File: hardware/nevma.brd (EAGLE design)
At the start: 34.6 x 15.9 mm, 9 parts, among them J1 USB_A_PTH_MALE, U1 TINY85-20-DIP

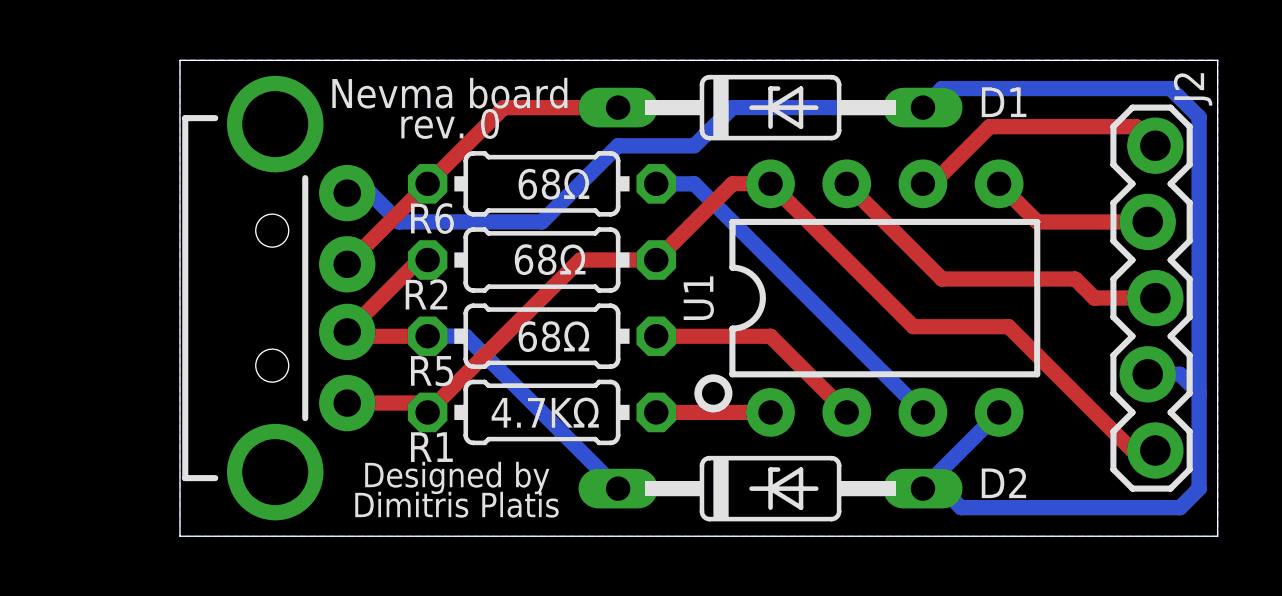
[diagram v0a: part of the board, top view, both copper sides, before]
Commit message: Decrease board size
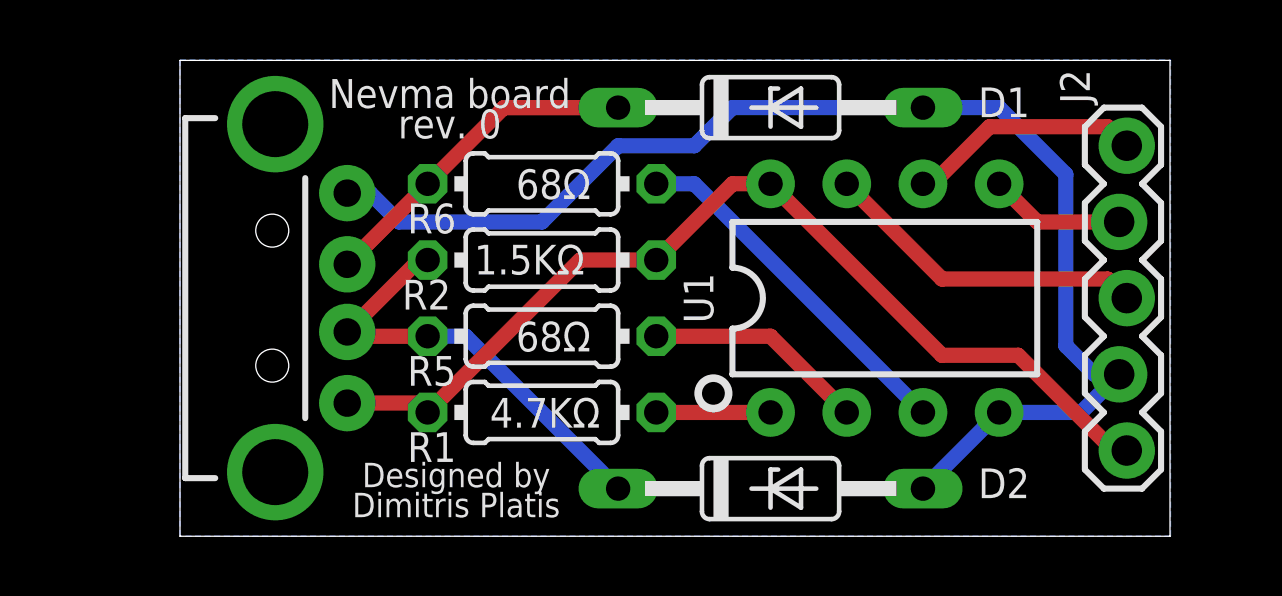
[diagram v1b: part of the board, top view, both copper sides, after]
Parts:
- R2: value 68Ω -> 1.5KΩ
- moved J2 0.95 mm to (70.2, 58.4)
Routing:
- net GND: track 58.7 -> 42.9 mm
- net VCC: track 33.9 -> 33.0 mm
- net SDA: track 5.48 -> 4.53 mm
- net SCL: track 11.9 -> 10.9 mm
- net INT: track 8.80 -> 7.85 mm
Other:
- board size 34.6 x 15.9 mm -> 33 x 15.9 mm
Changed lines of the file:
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@@
 <board>
 <plain>
-<wire x1="38.735" y1="45.4025" x2="73.3225" y2="45.4025" width="0" layer="20"/>
-<wire x1="73.3225" y1="45.4025" x2="73.3225" y2="61.265" width="0" layer="20"/>
-<wire x1="73.3225" y1="61.265" x2="38.735" y2="61.265" width="0" layer="20"/>
+<wire x1="38.735" y1="45.4025" x2="71.735" y2="45.4025" width="0" layer="20"/>
+<wire x1="71.735" y1="45.4025" x2="71.735" y2="61.265" width="0" layer="20"/>
+<wire x1="71.735" y1="61.265" x2="38.735" y2="61.265" width="0" layer="20"/>
 <wire x1="38.735" y1="61.265" x2="38.735" y2="45.4025" width="0" layer="20"/>
-<text x="72.39" y="48.895" size="8.636" layer="22" font="vector" ratio="20" distance="100" rot="MR0">NEVMA</text>
-<text x="47.7266" y="60.6425" size="0.9652" layer="21" font="vector" ratio="20" distance="5" align="top-center">Nevma board
+<text x="71.4375" y="48.895" size="8.636" layer="22" font="vector" ratio="20" distance="100" rot="MR0">NEVMA</text>
+<text x="47.7266" y="60.6425" size="0.9652" layer="21" font="vector" ratio="18" distance="5" align="top-center">Nevma board
 rev. 0</text>
 <text x="47.9425" y="46.0375" size="0.8128" layer="21" font="vector" ratio="10" distance="23" align="bottom-center">Designed by
@@
 <attribute name="VALUE" x="53.9115" y="45.4025" size="0.8128" layer="27" ratio="10"/>
 </element>
-<element name="J2" library="SparkFun-Connectors" library_urn="urn:adsk.eagle:library:513" package="1X05_LOCK" package3d_urn="urn:adsk.eagle:package:38105/1" value="" x="71.12" y="58.42" smashed="yes" rot="R270">
-<attribute name="NAME" x="71.882" y="60.96" size="0.9906" layer="25" font="vector" ratio="20" rot="R270"/>
-<attribute name="VALUE" x="69.088" y="59.69" size="0.6096" layer="27" font="vector" ratio="20" rot="R270"/>
+<element name="J2" library="SparkFun-Connectors" library_urn="urn:adsk.eagle:library:513" package="1X05_LOCK" package3d_urn="urn:adsk.eagle:package:38105/1" value="" x="70.1675" y="58.42" smashed="yes" rot="R270">
+<attribute name="NAME" x="68.072" y="60.96" size="0.9906" layer="25" font="vector" ratio="20" rot="R270"/>
+<attribute name="VALUE" x="68.1355" y="59.69" size="0.6096" layer="27" font="vector" ratio="20" rot="R270"/>
 </element>
 <element name="R1" library="rcl" library_urn="urn:adsk.eagle:library:334" package="0204/7" package3d_urn="urn:adsk.eagle:package:23498/1" value="4.7KΩ" x="50.8" y="49.53" smashed="yes" rot="R180">
@@
 <attribute name="VALUE" x="52.7431" y="50.0126" size="0.9906" layer="25" ratio="10" rot="R180"/>
 </element>
-<element name="R2" library="rcl" library_urn="urn:adsk.eagle:library:334" package="0204/7" package3d_urn="urn:adsk.eagle:package:23498/1" value="68Ω" x="50.8" y="54.61" smashed="yes">
+<element name="R2" library="rcl" library_urn="urn:adsk.eagle:library:334" package="0204/7" package3d_urn="urn:adsk.eagle:package:23498/1" value="1.5KΩ" x="50.8" y="54.61" smashed="yes">
 <attribute name="NAME" x="46.1391" y="52.959" size="0.9906" layer="25" ratio="10"/>
-<attribute name="VALUE" x="49.8094" y="54.1274" size="0.9906" layer="25" ratio="10"/>
+<attribute name="VALUE" x="48.5394" y="54.1274" size="0.9906" layer="25" ratio="10"/>
 </element>
 </elements>
@@
 <contactref element="J2" pad="4"/>
 <contactref element="U1" pad="4"/>
-<wire x1="66.04" y1="49.53" x2="63.5" y2="46.99" width="0.508" layer="16"/>
-<wire x1="72.0725" y1="46.355" x2="72.7075" y2="46.99" width="0.508" layer="16"/>
-<wire x1="72.7075" y1="46.99" x2="72.7075" y2="50.165" width="0.508" layer="16"/>
-<wire x1="72.7075" y1="50.165" x2="72.0725" y2="50.8" width="0.508" layer="16"/>
-<wire x1="72.0725" y1="50.8" x2="70.993" y2="50.8" width="0.508" layer="16"/>
-<wire x1="72.7075" y1="50.165" x2="72.7075" y2="59.3725" width="0.508" layer="16"/>
-<wire x1="72.7075" y1="59.3725" x2="71.755" y2="60.325" width="0.508" layer="16"/>
-<wire x1="71.755" y1="60.325" x2="64.135" y2="60.325" width="0.508" layer="16"/>
-<wire x1="63.5" y1="59.69" x2="64.135" y2="60.325" width="0.508" layer="16"/>
-<wire x1="63.5" y1="46.99" x2="64.135" y2="46.99" width="0.508" layer="16"/>
-<wire x1="64.135" y1="46.99" x2="64.77" y2="46.355" width="0.508" layer="16"/>
-<wire x1="64.77" y1="46.355" x2="72.0725" y2="46.355" width="0.508" layer="16"/>
+<wire x1="63.5" y1="46.99" x2="66.04" y2="49.53" width="0.508" layer="16"/>
 <wire x1="44.31" y1="56.84" x2="45.0775" y2="56.84" width="0.508" layer="16"/>
 <wire x1="45.0775" y1="56.84" x2="46.0375" y2="55.88" width="0.508" layer="16"/>
@@
 <wire x1="53.34" y1="58.42" x2="55.88" y2="58.42" width="0.508" layer="16"/>
 <wire x1="55.88" y1="58.42" x2="57.15" y2="59.69" width="0.508" layer="16"/>
-<wire x1="57.15" y1="59.69" x2="63.5" y2="59.69" width="0.508" layer="16"/>
+<wire x1="63.5" y1="59.69" x2="57.15" y2="59.69" width="0.508" layer="16"/>
+<wire x1="66.04" y1="49.53" x2="68.7705" y2="49.53" width="0.508" layer="16"/>
+<wire x1="68.7705" y1="49.53" x2="70.0405" y2="50.8" width="0.508" layer="16"/>
+<wire x1="70.0405" y1="50.8" x2="69.215" y2="50.8" width="0.508" layer="16"/>
+<wire x1="69.215" y1="50.8" x2="68.2625" y2="51.7525" width="0.508" layer="16"/>
+<wire x1="68.2625" y1="57.4675" x2="66.04" y2="59.69" width="0.508" layer="16"/>
+<wire x1="66.04" y1="59.69" x2="63.5" y2="59.69" width="0.508" layer="16"/>
+<wire x1="68.2625" y1="51.7525" x2="68.2625" y2="57.4675" width="0.508" layer="16"/>
 <polygon width="0.254" layer="16">
 <vertex x="38.735" y="61.2775"/>
-<vertex x="73.3425" y="61.2775"/>
-<vertex x="73.3425" y="45.4025"/>
+<vertex x="71.755" y="61.2775"/>
+<vertex x="71.755" y="45.4025"/>
 <vertex x="38.735" y="45.4025"/>
 </polygon>
@@
 <contactref element="R1" pad="2"/>
 <contactref element="R2" pad="2"/>
-<wire x1="71.247" y1="48.26" x2="70.485" y2="48.26" width="0.508" layer="1"/>
-<wire x1="70.485" y1="48.26" x2="66.3575" y2="52.3875" width="0.508" layer="1"/>
-<wire x1="66.3575" y1="52.3875" x2="63.1825" y2="52.3875" width="0.508" layer="1"/>
-<wire x1="63.1825" y1="52.3875" x2="58.42" y2="57.15" width="0.508" layer="1"/>
-<wire x1="44.31" y1="49.84" x2="46.68" y2="49.84" width="0.508" layer="1"/>
+<wire x1="46.68" y1="49.84" x2="44.31" y2="49.84" width="0.508" layer="1"/>
 <wire x1="46.99" y1="49.53" x2="46.68" y2="49.84" width="0.508" layer="1"/>
 <wire x1="58.42" y1="57.15" x2="57.15" y2="57.15" width="0.508" layer="1"/>
@@
 <wire x1="54.61" y1="54.61" x2="52.07" y2="54.61" width="0.508" layer="1"/>
 <wire x1="52.07" y1="54.61" x2="46.99" y2="49.53" width="0.508" layer="1"/>
+<wire x1="70.2945" y1="48.26" x2="69.85" y2="48.26" width="0.508" layer="1"/>
+<wire x1="69.85" y1="48.26" x2="66.675" y2="51.435" width="0.508" layer="1"/>
+<wire x1="66.675" y1="51.435" x2="64.135" y2="51.435" width="0.508" layer="1"/>
+<wire x1="64.135" y1="51.435" x2="58.42" y2="57.15" width="0.508" layer="1"/>
 </signal>
 <signal name="SDA">
 <contactref element="U1" pad="5"/>
 <contactref element="J2" pad="2"/>
-<wire x1="70.993" y1="55.88" x2="67.31" y2="55.88" width="0.508" layer="1"/>
-<wire x1="67.31" y1="55.88" x2="66.04" y2="57.15" width="0.508" layer="1"/>
+<wire x1="66.04" y1="57.15" x2="67.31" y2="55.88" width="0.508" layer="1"/>
+<wire x1="67.31" y1="55.88" x2="70.0405" y2="55.88" width="0.508" layer="1"/>
 </signal>
 <signal name="SCL">
 <contactref element="U1" pad="7"/>
 <contactref element="J2" pad="3"/>
-<wire x1="71.247" y1="53.34" x2="69.215" y2="53.34" width="0.508" layer="1"/>
-<wire x1="69.215" y1="53.34" x2="68.58" y2="53.975" width="0.508" layer="1"/>
-<wire x1="68.58" y1="53.975" x2="64.135" y2="53.975" width="0.508" layer="1"/>
-<wire x1="64.135" y1="53.975" x2="60.96" y2="57.15" width="0.508" layer="1"/>
+<wire x1="60.96" y1="57.15" x2="64.135" y2="53.975" width="0.508" layer="1"/>
+<wire x1="69.6595" y1="53.975" x2="70.2945" y2="53.34" width="0.508" layer="1"/>
+<wire x1="64.135" y1="53.975" x2="69.6595" y2="53.975" width="0.508" layer="1"/>
 </signal>
 <signal name="INT">
 <contactref element="J2" pad="1"/>
 <contactref element="U1" pad="6"/>
-<wire x1="71.247" y1="58.42" x2="70.612" y2="59.055" width="0.508" layer="1"/>
-<wire x1="70.612" y1="59.055" x2="65.7225" y2="59.055" width="0.508" layer="1"/>
+<wire x1="70.2945" y1="58.42" x2="69.6595" y2="59.055" width="0.508" layer="1"/>
+<wire x1="69.6595" y1="59.055" x2="65.7225" y2="59.055" width="0.508" layer="1"/>
 <wire x1="65.7225" y1="59.055" x2="63.8175" y2="57.15" width="0.508" layer="1"/>
 <wire x1="63.8175" y1="57.15" x2="63.5" y2="57.15" width="0.508" layer="1"/>

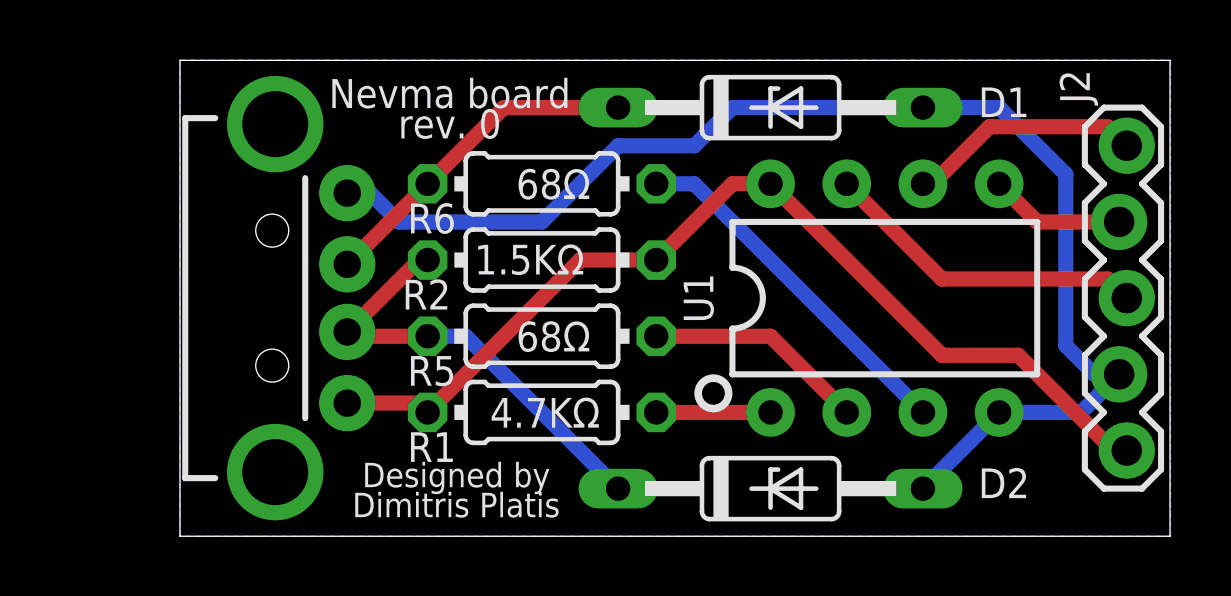
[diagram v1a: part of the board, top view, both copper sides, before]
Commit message: Reduce board size This will allower the better fit of the USB socket
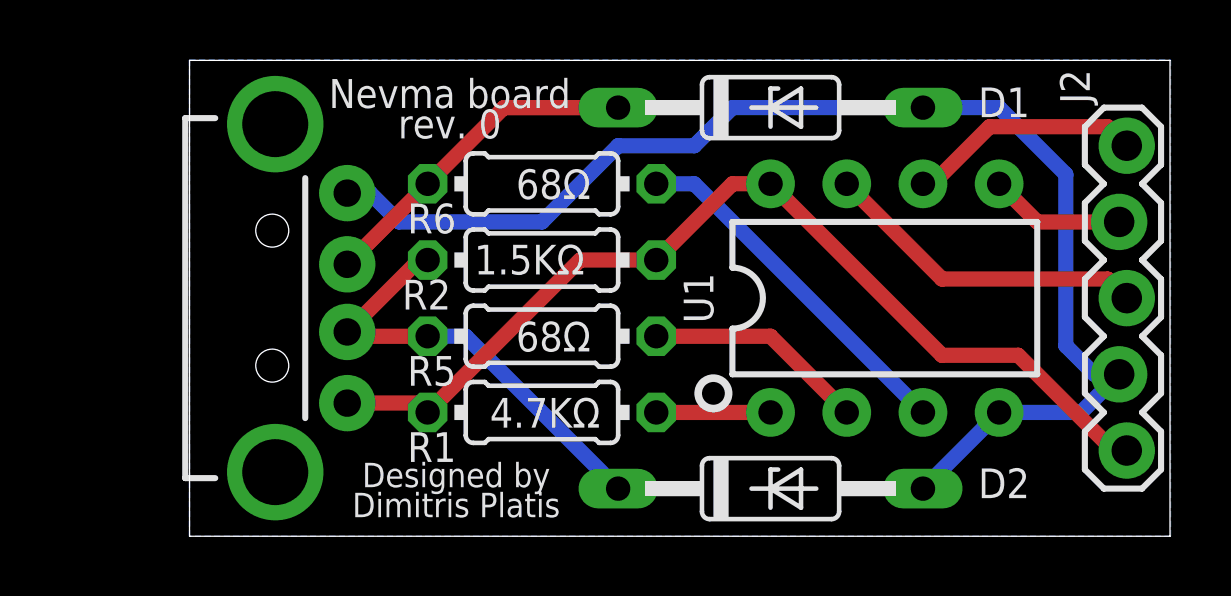
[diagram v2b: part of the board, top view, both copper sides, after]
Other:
- board size 33 x 15.9 mm -> 32.7 x 15.9 mm
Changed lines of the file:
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@@
 <board>
 <plain>
-<wire x1="38.735" y1="45.4025" x2="71.735" y2="45.4025" width="0" layer="20"/>
+<wire x1="39.0525" y1="45.4025" x2="71.735" y2="45.4025" width="0" layer="20"/>
 <wire x1="71.735" y1="45.4025" x2="71.735" y2="61.265" width="0" layer="20"/>
-<wire x1="71.735" y1="61.265" x2="38.735" y2="61.265" width="0" layer="20"/>
-<wire x1="38.735" y1="61.265" x2="38.735" y2="45.4025" width="0" layer="20"/>
+<wire x1="71.735" y1="61.265" x2="39.0525" y2="61.265" width="0" layer="20"/>
+<wire x1="39.0525" y1="61.265" x2="39.0525" y2="45.4025" width="0" layer="20"/>
 <text x="71.4375" y="48.895" size="8.636" layer="22" font="vector" ratio="20" distance="100" rot="MR0">NEVMA</text>
 <text x="47.7266" y="60.6425" size="0.9652" layer="21" font="vector" ratio="18" distance="5" align="top-center">Nevma board
@@
 <wire x1="68.2625" y1="51.7525" x2="68.2625" y2="57.4675" width="0.508" layer="16"/>
 <polygon width="0.254" layer="16">
-<vertex x="38.735" y="61.2775"/>
+<vertex x="39.0525" y="61.2775"/>
 <vertex x="71.755" y="61.2775"/>
 <vertex x="71.755" y="45.4025"/>
-<vertex x="38.735" y="45.4025"/>
+<vertex x="39.0525" y="45.4025"/>
 </polygon>
 </signal>

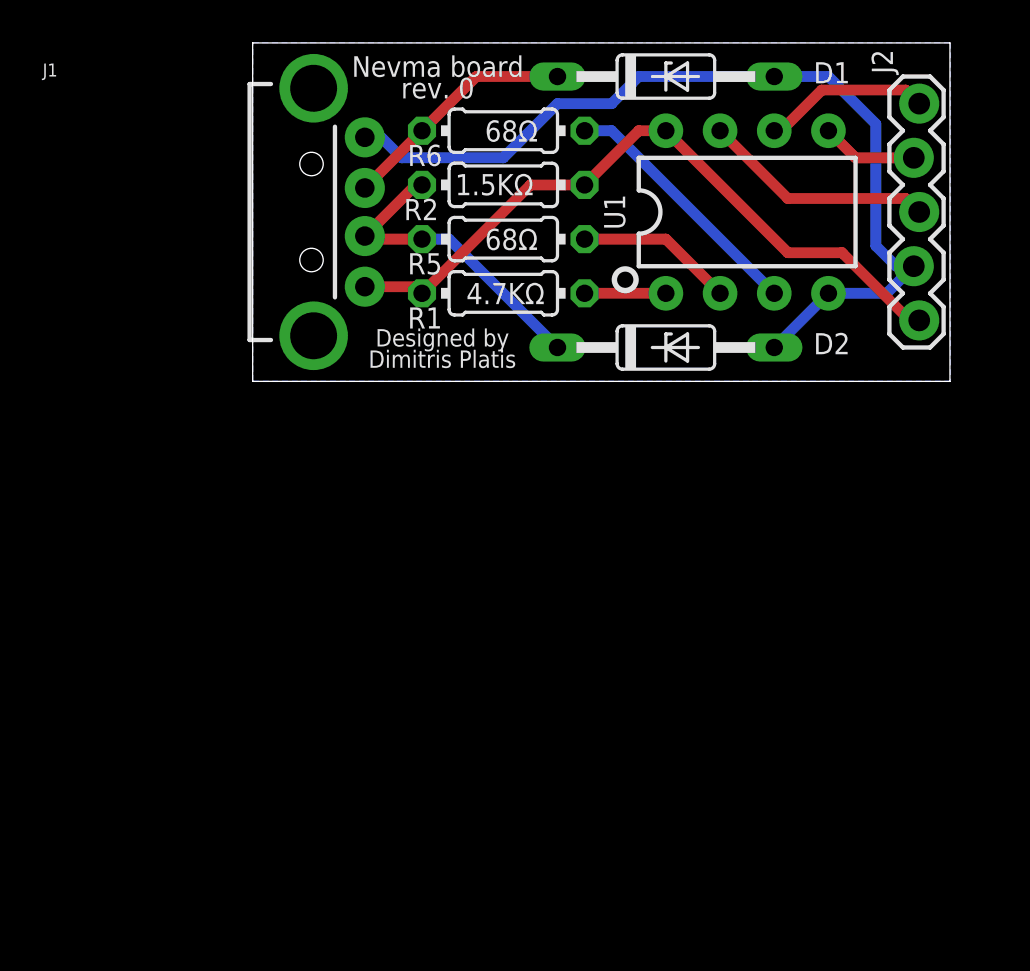
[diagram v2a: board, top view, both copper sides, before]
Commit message: New concept based on atmega32u4 board
HW rev. 2
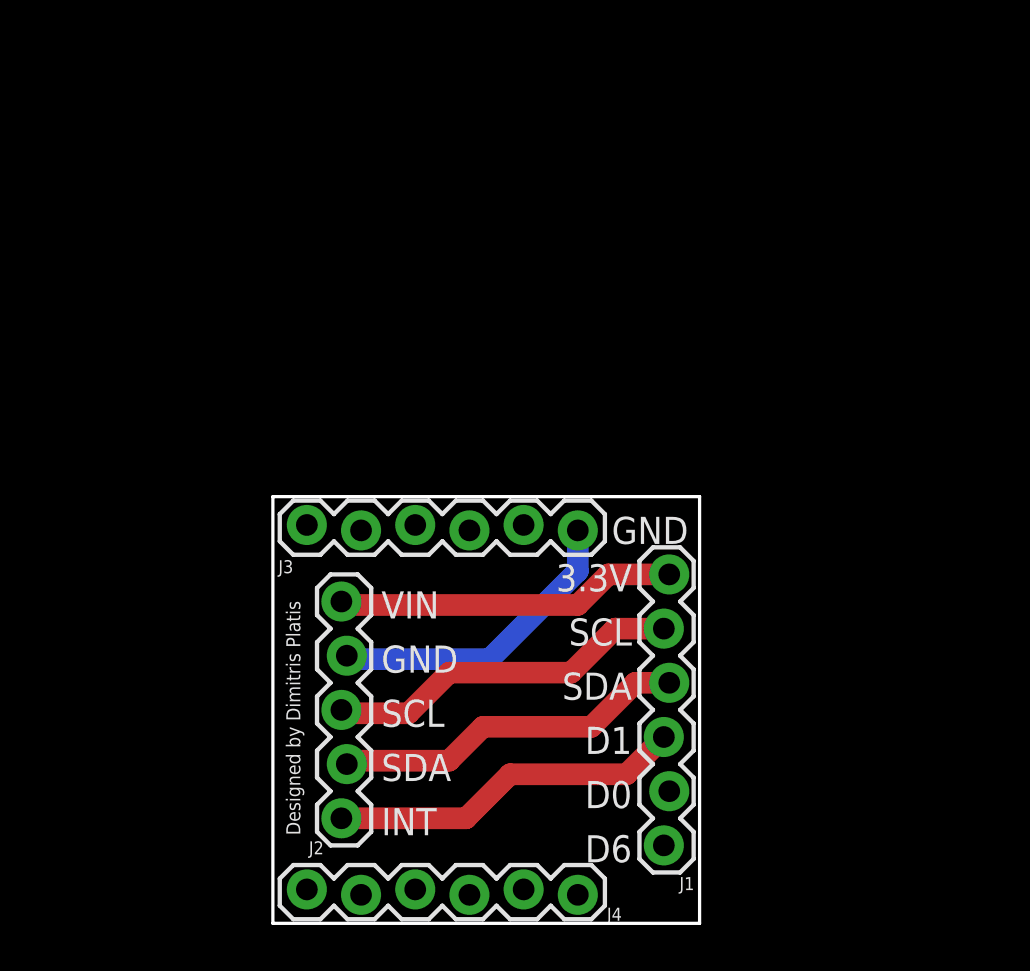
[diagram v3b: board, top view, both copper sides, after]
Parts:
- removed D1, D2: 3.6V, diode:DO35Z10
- removed R1: 4.7KΩ, rcl:0204/7
- removed R2: 1.5KΩ, rcl:0204/7
- removed R5, R6: 68Ω, rcl:0204/7
- removed U1: TINY85-20-DIP, SparkFun-Retired:DIP08_MCU
- added J3, J4: (no value), SparkFun-Connectors:1X06_LOCK
- J1: value USB_A_PTH_MALE -> (none); device SparkFun-Connectors:USB-A-H -> SparkFun-Connectors:1X06_LOCK
- moved J2 42.9 mm to (43.3, 24.9), turned to 90 degrees
- moved J1 23.8 mm to (58.6, 36.4), turned to 270 degrees
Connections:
- removed net N$1: R6.1, U1.3
- removed net N$2: R5.1, U1.2
- removed net N$3: D2.C, J1.D-, R2.1, R5.2
- removed net N$4: D1.C, J1.D+, R6.2
- removed net VCC: J1.VBUS, J2.5, R1.2, R2.2, U1.8
- new net 3.3V: J1.1, J2.5
- new net 5V: J3.2
- new net A0: J4.4
- new net A1: J4.5
- new net A2: J4.6
- new net D0: J1.5
- new net D10: J4.2
- new net D11: J4.1
- new net D14: J3.4
- new net D15: J3.5
- new net D16: J3.6
- new net D6: J1.6
- new net D9: J4.3
- net GND: now also J3.1; no longer D1.A, D2.A, J1.GND, U1.4
- net INT: now also J1.4; no longer U1.6
- net RST: now also J3.3; no longer R1.1, U1.1
- net SCL: now also J1.2; no longer U1.7
- net SDA: now also J1.3; no longer U1.5
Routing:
- net VCC: track 33.0 -> 0.00 mm
- net GND: track 42.9 -> 14.5 mm
- net 3.3V: track 0.00 -> 16.0 mm
- net N$3: track 14.9 -> 0.00 mm
- net SDA: track 4.53 -> 16.7 mm
- net N$1: track 12.0 -> 0.00 mm
- net N$4: track 11.2 -> 0.00 mm
- net INT: track 7.85 -> 16.7 mm
- net N$2: track 7.40 -> 0.00 mm
- net SCL: track 10.9 -> 16.8 mm
- net RST: track 3.81 -> 0.00 mm
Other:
- board size 32.7 x 15.9 mm -> 20 x 20 mm
- board text added: "3.3V SCL SDA D1 D0 D6"
- board text added: "GND"
- board text added: "Nevma board rev. 1"
- board text added: "VIN GND SCL SDA INT"
- board text removed: "NEVMA"
- board text removed: "Nevma board rev. 0"
